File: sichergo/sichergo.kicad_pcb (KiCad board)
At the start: 2 copper layers, 10 parts

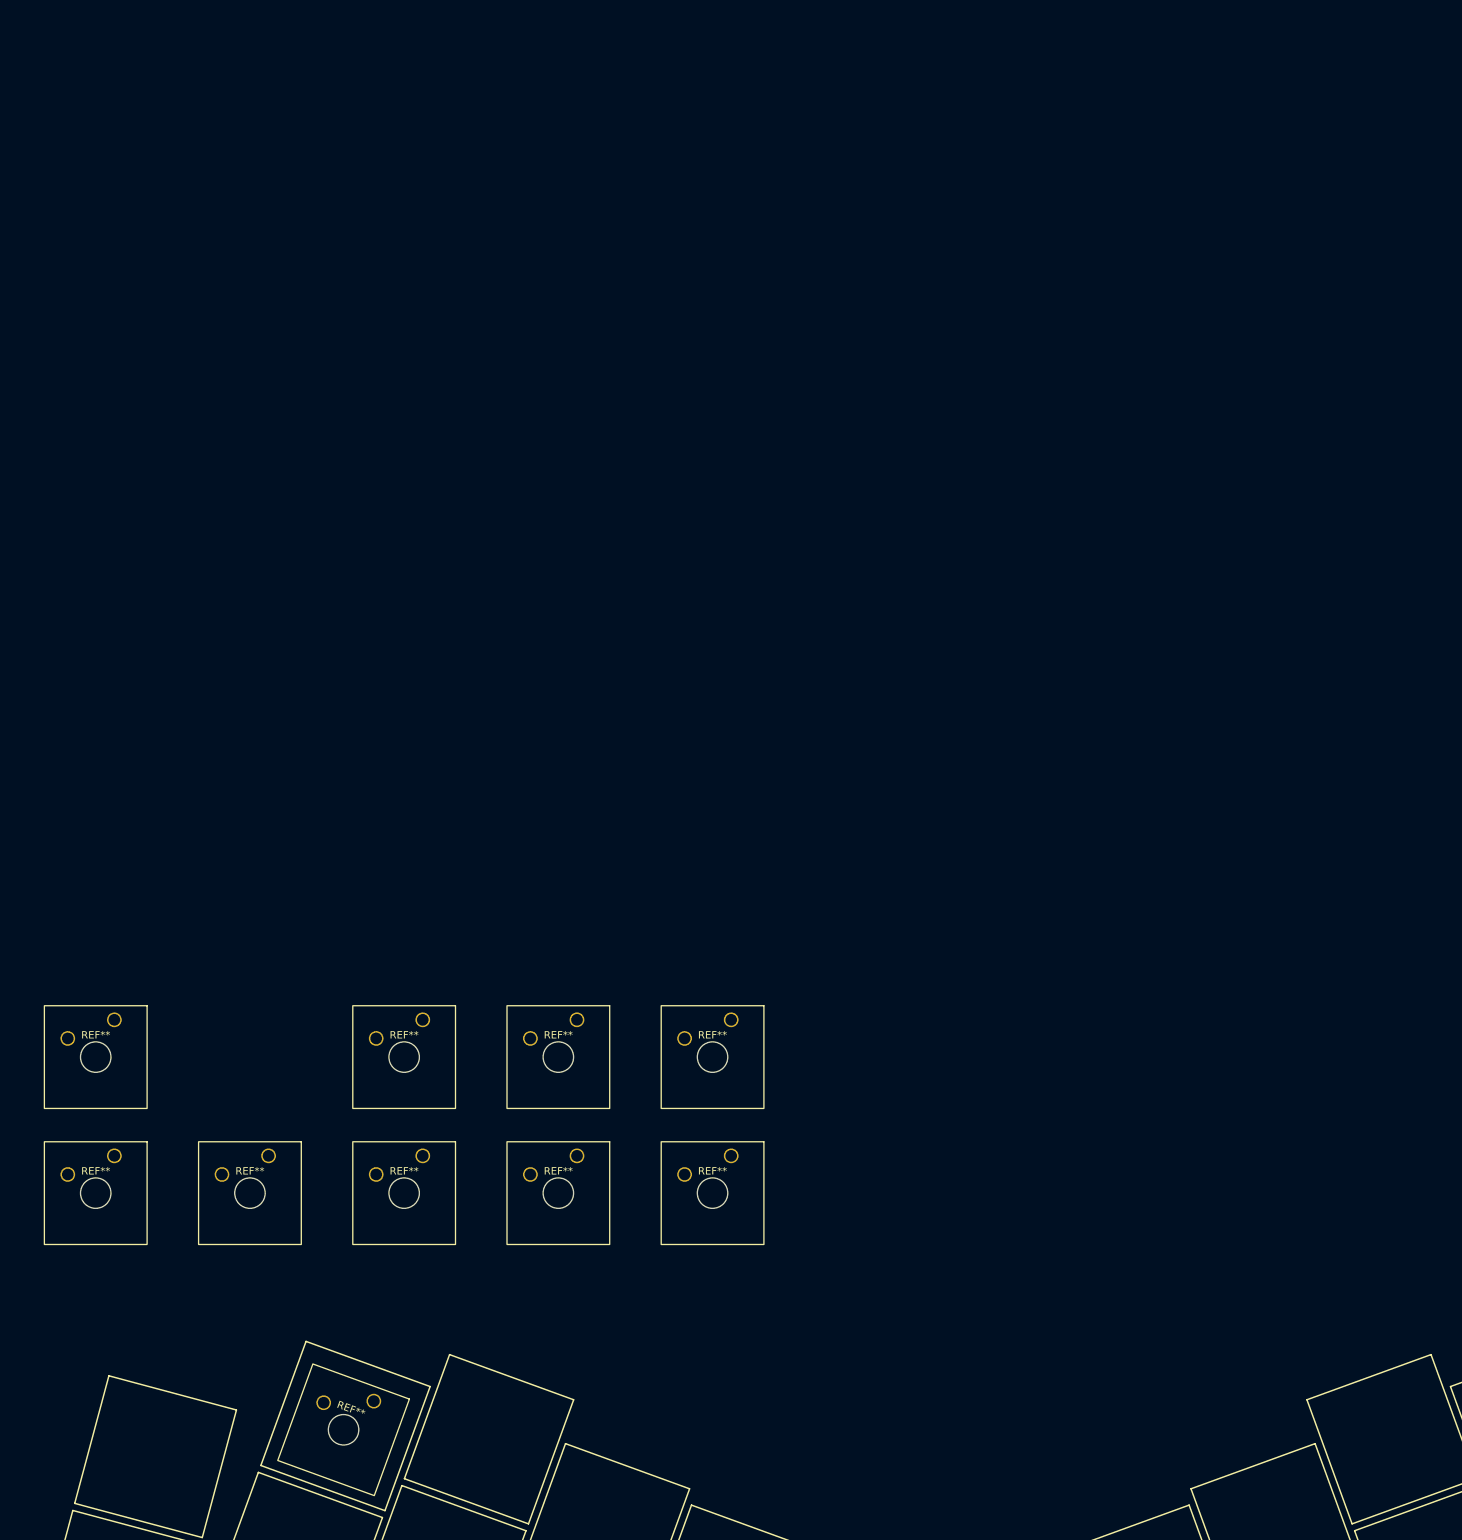
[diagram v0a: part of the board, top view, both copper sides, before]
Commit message: Added footprints to switches
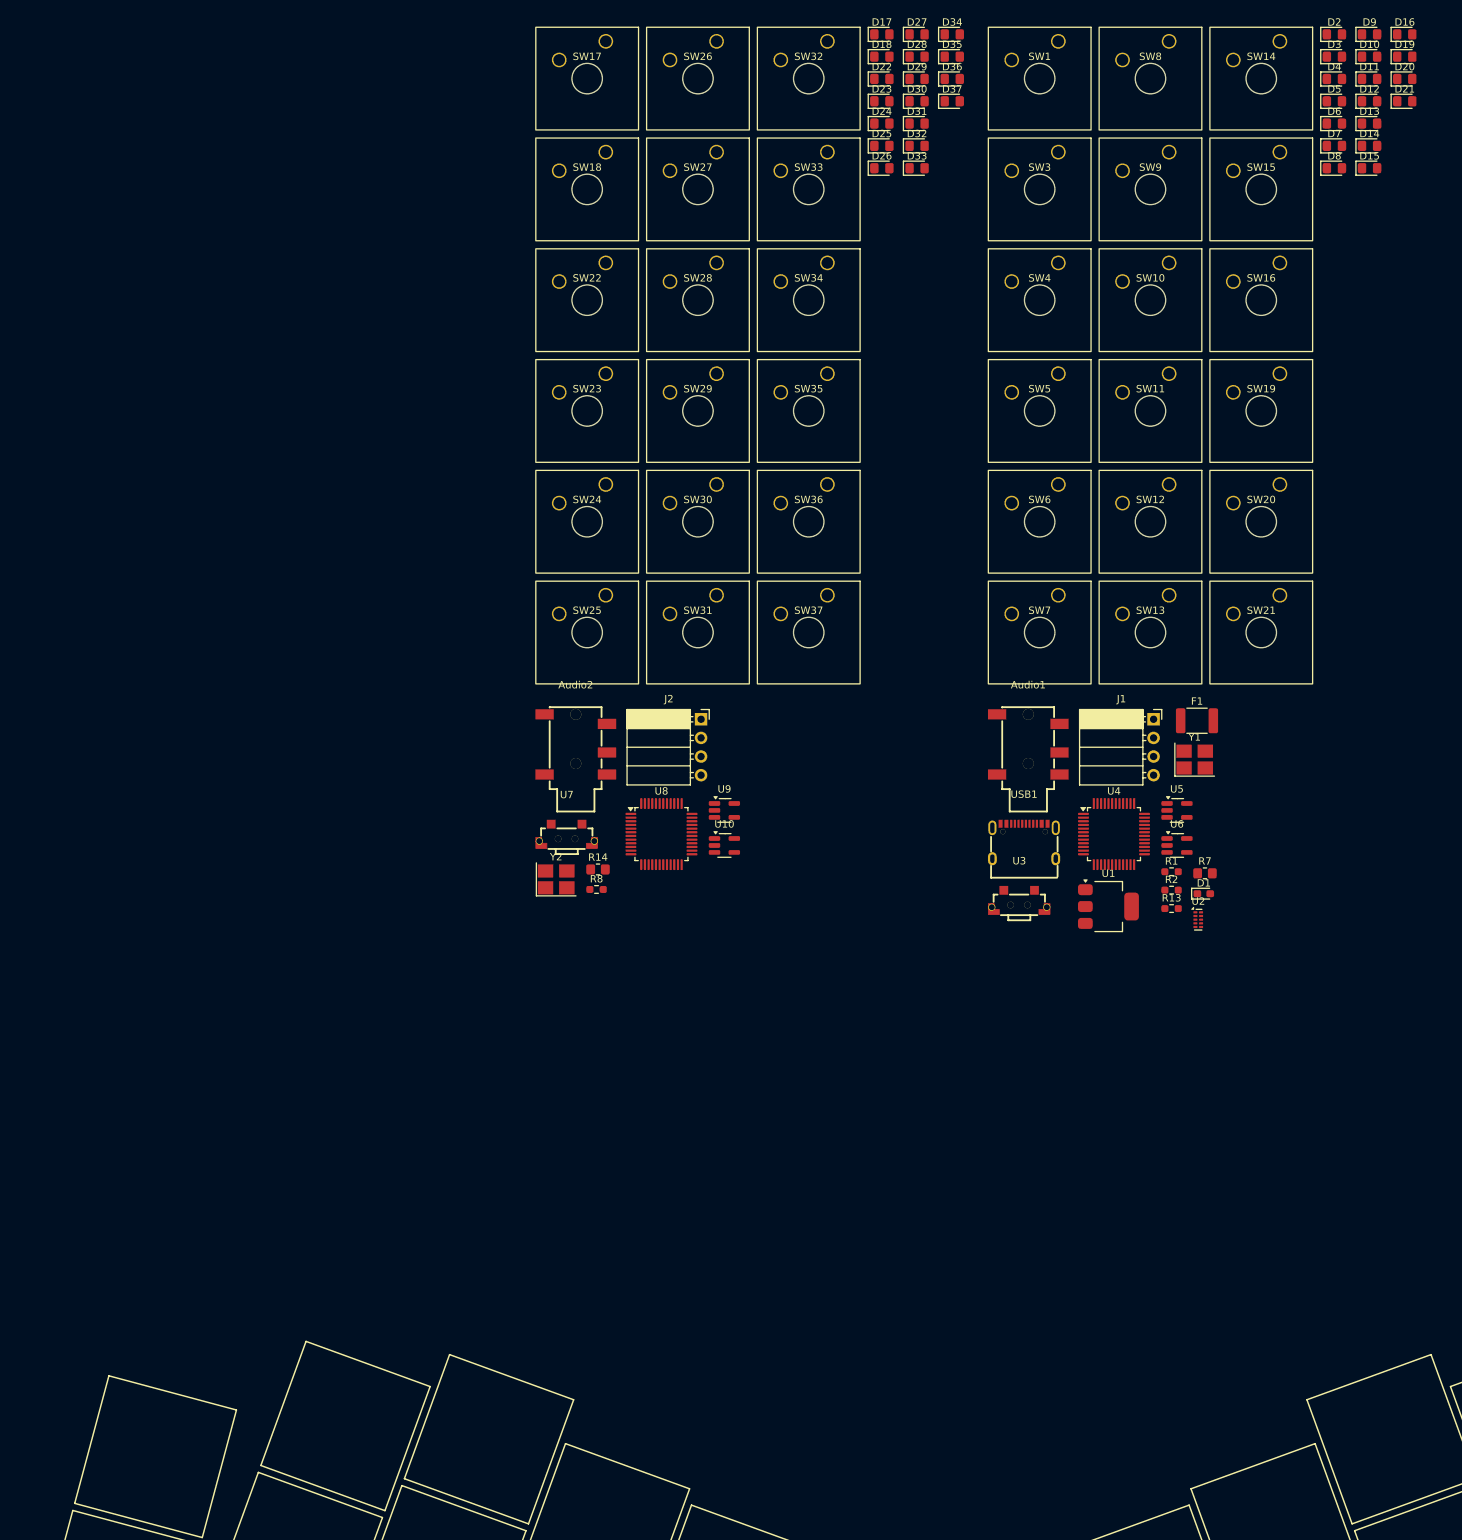
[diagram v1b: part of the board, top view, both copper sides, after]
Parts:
- removed REF** (x10): Gateron_Milky_Yellow, personal:Gateron_Milky_Yellow
- added Audio1: PJ-327E-SMT, easyeda2kicad:AUDIO-SMD_PJ-327E-SMT, F.Cu at (156.7, -28.5)
- added Audio2: PJ-327E-SMT, easyeda2kicad:AUDIO-SMD_PJ-327E-SMT, F.Cu at (95.0, -28.5)
- added D1: CPDUR5V0HE-HF, Diode_SMD:D_0603_1608Metric_Pad1.05x0.95mm_HandSolder, F.Cu at (180.6, -8.12)
- added D10: CD4148W, Diode_SMD:D_0805_2012Metric_Pad1.15x1.40mm_HandSolder, F.Cu at (203.2, -122.2)
- added D11: CD4148W, Diode_SMD:D_0805_2012Metric_Pad1.15x1.40mm_HandSolder, F.Cu at (203.2, -119.2)
- added D12: CD4148W, Diode_SMD:D_0805_2012Metric_Pad1.15x1.40mm_HandSolder, F.Cu at (203.2, -116.1)
- added D13: CD4148W, Diode_SMD:D_0805_2012Metric_Pad1.15x1.40mm_HandSolder, F.Cu at (203.2, -113.1)
- added D14: CD4148W, Diode_SMD:D_0805_2012Metric_Pad1.15x1.40mm_HandSolder, F.Cu at (203.2, -110.0)
- added D15: CD4148W, Diode_SMD:D_0805_2012Metric_Pad1.15x1.40mm_HandSolder, F.Cu at (203.2, -107.0)
- added D16: CD4148W, Diode_SMD:D_0805_2012Metric_Pad1.15x1.40mm_HandSolder, F.Cu at (208.0, -125.2)
- added D17: CD4148W, Diode_SMD:D_0805_2012Metric_Pad1.15x1.40mm_HandSolder, F.Cu at (136.8, -125.2)
- added D18: CD4148W, Diode_SMD:D_0805_2012Metric_Pad1.15x1.40mm_HandSolder, F.Cu at (136.8, -122.2)
- added D19: CD4148W, Diode_SMD:D_0805_2012Metric_Pad1.15x1.40mm_HandSolder, F.Cu at (208.0, -122.2)
- added D2: CD4148W, Diode_SMD:D_0805_2012Metric_Pad1.15x1.40mm_HandSolder, F.Cu at (198.4, -125.2)
- added D20: CD4148W, Diode_SMD:D_0805_2012Metric_Pad1.15x1.40mm_HandSolder, F.Cu at (208.0, -119.2)
- added D21: CD4148W, Diode_SMD:D_0805_2012Metric_Pad1.15x1.40mm_HandSolder, F.Cu at (208.0, -116.1)
- added D22: CD4148W, Diode_SMD:D_0805_2012Metric_Pad1.15x1.40mm_HandSolder, F.Cu at (136.8, -119.2)
- added D23: CD4148W, Diode_SMD:D_0805_2012Metric_Pad1.15x1.40mm_HandSolder, F.Cu at (136.8, -116.1)
- added D24: CD4148W, Diode_SMD:D_0805_2012Metric_Pad1.15x1.40mm_HandSolder, F.Cu at (136.8, -113.1)
- added D25: CD4148W, Diode_SMD:D_0805_2012Metric_Pad1.15x1.40mm_HandSolder, F.Cu at (136.8, -110.0)
- added D26: CD4148W, Diode_SMD:D_0805_2012Metric_Pad1.15x1.40mm_HandSolder, F.Cu at (136.8, -107.0)
- added D27: CD4148W, Diode_SMD:D_0805_2012Metric_Pad1.15x1.40mm_HandSolder, F.Cu at (141.6, -125.2)
- added D28: CD4148W, Diode_SMD:D_0805_2012Metric_Pad1.15x1.40mm_HandSolder, F.Cu at (141.6, -122.2)
- added D29: CD4148W, Diode_SMD:D_0805_2012Metric_Pad1.15x1.40mm_HandSolder, F.Cu at (141.6, -119.2)
- added D3: CD4148W, Diode_SMD:D_0805_2012Metric_Pad1.15x1.40mm_HandSolder, F.Cu at (198.4, -122.2)
- added D30: CD4148W, Diode_SMD:D_0805_2012Metric_Pad1.15x1.40mm_HandSolder, F.Cu at (141.6, -116.1)
- added D31: CD4148W, Diode_SMD:D_0805_2012Metric_Pad1.15x1.40mm_HandSolder, F.Cu at (141.6, -113.1)
- added D32: CD4148W, Diode_SMD:D_0805_2012Metric_Pad1.15x1.40mm_HandSolder, F.Cu at (141.6, -110.0)
- added D33: CD4148W, Diode_SMD:D_0805_2012Metric_Pad1.15x1.40mm_HandSolder, F.Cu at (141.6, -107.0)
- added D34: CD4148W, Diode_SMD:D_0805_2012Metric_Pad1.15x1.40mm_HandSolder, F.Cu at (146.3, -125.2)
- added D35: CD4148W, Diode_SMD:D_0805_2012Metric_Pad1.15x1.40mm_HandSolder, F.Cu at (146.3, -122.2)
- added D36: CD4148W, Diode_SMD:D_0805_2012Metric_Pad1.15x1.40mm_HandSolder, F.Cu at (146.3, -119.2)
- added D37: CD4148W, Diode_SMD:D_0805_2012Metric_Pad1.15x1.40mm_HandSolder, F.Cu at (146.3, -116.1)
- added D4: CD4148W, Diode_SMD:D_0805_2012Metric_Pad1.15x1.40mm_HandSolder, F.Cu at (198.4, -119.2)
- added D5: CD4148W, Diode_SMD:D_0805_2012Metric_Pad1.15x1.40mm_HandSolder, F.Cu at (198.4, -116.1)
- added D6: CD4148W, Diode_SMD:D_0805_2012Metric_Pad1.15x1.40mm_HandSolder, F.Cu at (198.4, -113.1)
- added D7: CD4148W, Diode_SMD:D_0805_2012Metric_Pad1.15x1.40mm_HandSolder, F.Cu at (198.4, -110.0)
- added D8: CD4148W, Diode_SMD:D_0805_2012Metric_Pad1.15x1.40mm_HandSolder, F.Cu at (198.4, -107.0)
- added D9: CD4148W, Diode_SMD:D_0805_2012Metric_Pad1.15x1.40mm_HandSolder, F.Cu at (203.2, -125.2)
- added F1: 1812L050/30PR, Fuse:Fuse_1812_4532Metric_Pad1.30x3.40mm_HandSolder, F.Cu at (179.7, -31.7)
- added J1: Conn_01x04_Pin, Connector_PinSocket_2.54mm:PinSocket_1x04_P2.54mm_Horizontal, F.Cu at (173.8, -31.9)
- added J2: Conn_01x04_Pin, Connector_PinSocket_2.54mm:PinSocket_1x04_P2.54mm_Horizontal, F.Cu at (112.1, -31.9)
- added R1: 5.1 kohm, Resistor_SMD:R_0603_1608Metric_Pad0.98x0.95mm_HandSolder, F.Cu at (176.2, -11.1)
- added R13: 5.1 kohm, Resistor_SMD:R_0603_1608Metric_Pad0.98x0.95mm_HandSolder, F.Cu at (176.2, -6.09)
- added R14: 100 ohm, Resistor_SMD:R_0805_2012Metric_Pad1.20x1.40mm_HandSolder, F.Cu at (98.1, -11.4)
- added R2: 4.7 kohm, Resistor_SMD:R_0603_1608Metric_Pad0.98x0.95mm_HandSolder, F.Cu at (176.2, -8.60)
- added R7: 100 ohm, Resistor_SMD:R_0805_2012Metric_Pad1.20x1.40mm_HandSolder, F.Cu at (180.8, -10.9)
- added R8: 4.7 kohm, Resistor_SMD:R_0603_1608Metric_Pad0.98x0.95mm_HandSolder, F.Cu at (97.9, -8.69)
- added SW1: SW_Push, personal:Gateron_Milky_Yellow, F.Cu at (158.3, -119.2)
- added SW10: SW_Push, personal:Gateron_Milky_Yellow, F.Cu at (173.4, -89.0)
- added SW11: SW_Push, personal:Gateron_Milky_Yellow, F.Cu at (173.4, -73.9)
- added SW12: SW_Push, personal:Gateron_Milky_Yellow, F.Cu at (173.4, -58.8)
- added SW13: SW_Push, personal:Gateron_Milky_Yellow, F.Cu at (173.4, -43.7)
- added SW14: SW_Push, personal:Gateron_Milky_Yellow, F.Cu at (188.5, -119.2)
- added SW15: SW_Push, personal:Gateron_Milky_Yellow, F.Cu at (188.5, -104.1)
- added SW16: SW_Push, personal:Gateron_Milky_Yellow, F.Cu at (188.5, -89.0)
- added SW17: SW_Push, personal:Gateron_Milky_Yellow, F.Cu at (96.6, -119.2)
- added SW18: SW_Push, personal:Gateron_Milky_Yellow, F.Cu at (96.6, -104.1)
- added SW19: SW_Push, personal:Gateron_Milky_Yellow, F.Cu at (188.5, -73.9)
- added SW20: SW_Push, personal:Gateron_Milky_Yellow, F.Cu at (188.5, -58.8)
- added SW21: SW_Push, personal:Gateron_Milky_Yellow, F.Cu at (188.5, -43.7)
- added SW22: SW_Push, personal:Gateron_Milky_Yellow, F.Cu at (96.6, -89.0)
- added SW23: SW_Push, personal:Gateron_Milky_Yellow, F.Cu at (96.6, -73.9)
- added SW24: SW_Push, personal:Gateron_Milky_Yellow, F.Cu at (96.6, -58.8)
- added SW25: SW_Push, personal:Gateron_Milky_Yellow, F.Cu at (96.6, -43.7)
- added SW26: SW_Push, personal:Gateron_Milky_Yellow, F.Cu at (111.7, -119.2)
- added SW27: SW_Push, personal:Gateron_Milky_Yellow, F.Cu at (111.7, -104.1)
- added SW28: SW_Push, personal:Gateron_Milky_Yellow, F.Cu at (111.7, -89.0)
- added SW29: SW_Push, personal:Gateron_Milky_Yellow, F.Cu at (111.7, -73.9)
- added SW3: SW_Push, personal:Gateron_Milky_Yellow, F.Cu at (158.3, -104.1)
- added SW30: SW_Push, personal:Gateron_Milky_Yellow, F.Cu at (111.7, -58.8)
- added SW31: SW_Push, personal:Gateron_Milky_Yellow, F.Cu at (111.7, -43.7)
- added SW32: SW_Push, personal:Gateron_Milky_Yellow, F.Cu at (126.8, -119.2)
- added SW33: SW_Push, personal:Gateron_Milky_Yellow, F.Cu at (126.8, -104.1)
- added SW34: SW_Push, personal:Gateron_Milky_Yellow, F.Cu at (126.8, -89.0)
- added SW35: SW_Push, personal:Gateron_Milky_Yellow, F.Cu at (126.8, -73.9)
- added SW36: SW_Push, personal:Gateron_Milky_Yellow, F.Cu at (126.8, -58.8)
- added SW37: SW_Push, personal:Gateron_Milky_Yellow, F.Cu at (126.8, -43.7)
- added SW4: SW_Push, personal:Gateron_Milky_Yellow, F.Cu at (158.3, -89.0)
- added SW5: SW_Push, personal:Gateron_Milky_Yellow, F.Cu at (158.3, -73.9)
- added SW6: SW_Push, personal:Gateron_Milky_Yellow, F.Cu at (158.3, -58.8)
- added SW7: SW_Push, personal:Gateron_Milky_Yellow, F.Cu at (158.3, -43.7)
- added SW8: SW_Push, personal:Gateron_Milky_Yellow, F.Cu at (173.4, -119.2)
- added SW9: SW_Push, personal:Gateron_Milky_Yellow, F.Cu at (173.4, -104.1)
- added U1: AZ1117-3.3, Package_TO_SOT_SMD:SOT-223-3_TabPin2, F.Cu at (167.6, -6.36)
- added U10: SN74LVC1G125DBV, Package_TO_SOT_SMD:SOT-23-5_HandSoldering, F.Cu at (115.3, -14.7)
- added U2: TPD4E05U06DQA, Package_SON:USON-10_2.5x1.0mm_P0.5mm, F.Cu at (179.9, -4.57)
- added U3: YTS1C0033BBG01, easyeda2kicad:SW-SMD_YIYUAN_YTS1C003XXX, F.Cu at (155.5, -7.29)
- added U4: STM32F103C8Tx, Package_QFP:LQFP-48_7x7mm_P0.5mm, F.Cu at (168.4, -16.2)
- added U5: SN74LVC1G125DBV, Package_TO_SOT_SMD:SOT-23-5_HandSoldering, F.Cu at (177.0, -19.5)
- added U6: SN74LVC1G125DBV, Package_TO_SOT_SMD:SOT-23-5_HandSoldering, F.Cu at (177.0, -14.7)
- added U7: YTS1C0033BBG01, easyeda2kicad:SW-SMD_YIYUAN_YTS1C003XXX, F.Cu at (93.8, -16.3)
- added U8: STM32F103C8Tx, Package_QFP:LQFP-48_7x7mm_P0.5mm, F.Cu at (106.7, -16.2)
- added U9: SN74LVC1G125DBV, Package_TO_SOT_SMD:SOT-23-5_HandSoldering, F.Cu at (115.3, -19.5)
- added USB1: TYPE-C 16PIN 2MD(073), easyeda2kicad:USB-C-SMD_TYPE-C-6PIN-2MD-073, F.Cu at (156.1, -15.3)
- added Y1: Crystal_GND24, Crystal:Crystal_SMD_3225-4Pin_3.2x2.5mm_HandSoldering, F.Cu at (179.4, -26.4)
- added Y2: Crystal_GND24, Crystal:Crystal_SMD_3225-4Pin_3.2x2.5mm_HandSoldering, F.Cu at (92.4, -10.1)

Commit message: Add backlight and switch connections
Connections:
- Audio1 pad 1: +3V3 -> Net-(Audio1-Pad1)
- Audio1 pad 2: Net-(Audio1-Pad2) -> +3V3
- Audio1 pad 5: Net-(Audio1-Pad2) -> +3V3
- Audio2 pad 1: +3V3 -> Net-(Audio2-Pad1)
- Audio2 pad 2: Net-(Audio2-Pad2) -> +3V3
- Audio2 pad 5: Net-(Audio2-Pad2) -> +3V3
- D10 pad 1: /KBD_L/MatrixL/KB_ROW_1 -> /KBD_L/KB_ROW_1
- D11 pad 1: /KBD_L/MatrixL/KB_ROW_1 -> /KBD_L/KB_ROW_1
- D12 pad 1: /KBD_L/MatrixL/KB_ROW_2 -> /KBD_L/KB_ROW_2
- D13 pad 1: /KBD_L/MatrixL/KB_ROW_2 -> /KBD_L/KB_ROW_2
- D14 pad 1: /KBD_L/MatrixL/KB_ROW_2 -> /KBD_L/KB_ROW_2
- D15 pad 1: /KBD_L/MatrixL/KB_ROW_2 -> /KBD_L/KB_ROW_2
- D16 pad 1: /KBD_L/MatrixL/KB_ROW_2 -> /KBD_L/KB_ROW_2
- D17 pad 1: /KBD_R/MatrixR/KB_ROW_4 -> /KBD_R/KB_ROW_4
- D18 pad 1: /KBD_R/MatrixR/KB_COL_5 -> /KBD_R/KB_ROW_5
- D19 pad 1: /KBD_L/MatrixL/KB_ROW_3 -> /KBD_L/KB_ROW_3
- D2 pad 1: /KBD_L/MatrixL/KB_ROW_0 -> /KBD_L/KB_ROW_0
- D20 pad 1: /KBD_L/MatrixL/KB_ROW_3 -> /KBD_L/KB_ROW_3
- D21 pad 1: /KBD_L/MatrixL/KB_ROW_3 -> /KBD_L/KB_ROW_3
- D22 pad 1: /KBD_R/MatrixR/KB_COL_6 -> /KBD_R/KB_ROW_6
- D23 pad 1: /KBD_R/MatrixR/KB_ROW_4 -> /KBD_R/KB_ROW_4
- D24 pad 1: /KBD_R/MatrixR/KB_COL_5 -> /KBD_R/KB_ROW_5
- D25 pad 1: /KBD_R/MatrixR/KB_COL_6 -> /KBD_R/KB_ROW_6
- D26 pad 1: /KBD_R/MatrixR/KB_ROW_4 -> /KBD_R/KB_ROW_4
- D27 pad 1: /KBD_R/MatrixR/KB_COL_5 -> /KBD_R/KB_ROW_5
- D28 pad 1: /KBD_R/MatrixR/KB_COL_6 -> /KBD_R/KB_ROW_6
- D29 pad 1: /KBD_R/MatrixR/KB_COL_7 -> /KBD_R/KB_ROW_7
- D3 pad 1: /KBD_L/MatrixL/KB_ROW_0 -> /KBD_L/KB_ROW_0
- D30 pad 1: /KBD_R/MatrixR/KB_ROW_4 -> /KBD_R/KB_ROW_4
- D31 pad 1: /KBD_R/MatrixR/KB_COL_5 -> /KBD_R/KB_ROW_5
- D32 pad 1: /KBD_R/MatrixR/KB_COL_6 -> /KBD_R/KB_ROW_6
- D33 pad 1: /KBD_R/MatrixR/KB_COL_7 -> /KBD_R/KB_ROW_7
- D34 pad 1: /KBD_R/MatrixR/KB_ROW_4 -> /KBD_R/KB_ROW_4
- D35 pad 1: /KBD_R/MatrixR/KB_COL_5 -> /KBD_R/KB_ROW_5
- D36 pad 1: /KBD_R/MatrixR/KB_COL_6 -> /KBD_R/KB_ROW_6
- D37 pad 1: /KBD_R/MatrixR/KB_COL_7 -> /KBD_R/KB_ROW_7
- D4 pad 1: /KBD_L/MatrixL/KB_ROW_0 -> /KBD_L/KB_ROW_0
- D5 pad 1: /KBD_L/MatrixL/KB_ROW_0 -> /KBD_L/KB_ROW_0
- D6 pad 1: /KBD_L/MatrixL/KB_ROW_0 -> /KBD_L/KB_ROW_0
- D7 pad 1: /KBD_L/MatrixL/KB_ROW_1 -> /KBD_L/KB_ROW_1
- D8 pad 1: /KBD_L/MatrixL/KB_ROW_1 -> /KBD_L/KB_ROW_1
- D9 pad 1: /KBD_L/MatrixL/KB_ROW_1 -> /KBD_L/KB_ROW_1
- R14 pad 1: Net-(Audio2-Pad2) -> Net-(Audio2-Pad1)
- R7 pad 1: Net-(Audio1-Pad2) -> Net-(Audio1-Pad1)
- SW1 pad 1: /KBD_L/MatrixL/KB_COL_0 -> /KBD_L/KB_COL_0
- SW10 pad 1: /KBD_L/MatrixL/KB_COL_3 -> /KBD_L/KB_COL_3
- SW11 pad 1: /KBD_L/MatrixL/KB_COL_4 -> /KBD_L/KB_COL_4
- SW12 pad 1: /KBD_L/MatrixL/KB_COL_0 -> /KBD_L/KB_COL_0
- SW13 pad 1: /KBD_L/MatrixL/KB_COL_1 -> /KBD_L/KB_COL_1
- SW14 pad 1: /KBD_L/MatrixL/KB_COL_2 -> /KBD_L/KB_COL_2
- SW15 pad 1: /KBD_L/MatrixL/KB_COL_3 -> /KBD_L/KB_COL_3
- SW16 pad 1: /KBD_L/MatrixL/KB_COL_4 -> /KBD_L/KB_COL_4
- SW17 pad 1: /KBD_R/MatrixR/KB_COL_0 -> /KBD_R/KB_COL_0
- SW18 pad 1: /KBD_R/MatrixR/KB_COL_0 -> /KBD_R/KB_COL_0
- SW19 pad 1: /KBD_L/MatrixL/KB_COL_2 -> /KBD_L/KB_COL_2
- SW20 pad 1: /KBD_L/MatrixL/KB_COL_3 -> /KBD_L/KB_COL_3
- SW21 pad 1: /KBD_L/MatrixL/KB_COL_4 -> /KBD_L/KB_COL_4
- SW22 pad 1: /KBD_R/MatrixR/KB_COL_0 -> /KBD_R/KB_COL_0
- SW23 pad 1: /KBD_R/MatrixR/KB_COL_1 -> /KBD_R/KB_COL_1
- SW24 pad 1: /KBD_R/MatrixR/KB_COL_1 -> /KBD_R/KB_COL_1
- SW25 pad 1: /KBD_R/MatrixR/KB_COL_1 -> /KBD_R/KB_COL_1
- SW26 pad 1: /KBD_R/MatrixR/KB_COL_2 -> /KBD_R/KB_COL_2
- SW27 pad 1: /KBD_R/MatrixR/KB_COL_2 -> /KBD_R/KB_COL_2
- SW28 pad 1: /KBD_R/MatrixR/KB_COL_2 -> /KBD_R/KB_COL_2
- SW29 pad 1: /KBD_R/MatrixR/KB_COL_0 -> /KBD_R/KB_COL_0
- SW3 pad 1: /KBD_L/MatrixL/KB_COL_1 -> /KBD_L/KB_COL_1
- SW30 pad 1: /KBD_R/MatrixR/KB_COL_3 -> /KBD_R/KB_COL_3
- SW31 pad 1: /KBD_R/MatrixR/KB_COL_3 -> /KBD_R/KB_COL_3
- SW32 pad 1: /KBD_R/MatrixR/KB_COL_3 -> /KBD_R/KB_COL_3
- SW33 pad 1: /KBD_R/MatrixR/KB_COL_1 -> /KBD_R/KB_COL_1
- SW34 pad 1: /KBD_R/MatrixR/KB_COL_4 -> /KBD_R/KB_COL_4
- SW35 pad 1: /KBD_R/MatrixR/KB_COL_4 -> /KBD_R/KB_COL_4
- SW36 pad 1: /KBD_R/MatrixR/KB_COL_4 -> /KBD_R/KB_COL_4
- SW37 pad 1: /KBD_R/MatrixR/KB_COL_2 -> /KBD_R/KB_COL_2
- SW4 pad 1: /KBD_L/MatrixL/KB_COL_2 -> /KBD_L/KB_COL_2
- SW5 pad 1: /KBD_L/MatrixL/KB_COL_3 -> /KBD_L/KB_COL_3
- SW6 pad 1: /KBD_L/MatrixL/KB_COL_4 -> /KBD_L/KB_COL_4
- SW7 pad 1: /KBD_L/MatrixL/KB_COL_0 -> /KBD_L/KB_COL_0
- SW8 pad 1: /KBD_L/MatrixL/KB_COL_1 -> /KBD_L/KB_COL_1
- SW9 pad 1: /KBD_L/MatrixL/KB_COL_2 -> /KBD_L/KB_COL_2
- U4 pad 10: unconnected-(U4-PA0-Pad10) -> /KBD_L/KB_COL_0
- U4 pad 11: unconnected-(U4-PA1-Pad11) -> /KBD_L/KB_COL_1
- U4 pad 12: unconnected-(U4-PA2-Pad12) -> /KBD_L/KB_COL_2
- U4 pad 13: unconnected-(U4-PA3-Pad13) -> /KBD_L/KB_COL_3
- U4 pad 14: unconnected-(U4-PA4-Pad14) -> /KBD_L/KB_COL_4
- U4 pad 15: unconnected-(U4-PA5-Pad15) -> /KBD_L/KB_ROW_0
- U4 pad 16: unconnected-(U4-PA6-Pad16) -> /KBD_L/KB_ROW_1
- U4 pad 17: unconnected-(U4-PA7-Pad17) -> /KBD_L/KB_ROW_2
- U4 pad 29: unconnected-(U4-PA8-Pad29) -> /KBD_L/KB_ROW_3
- U8 pad 10: unconnected-(U8-PA0-Pad10) -> /KBD_R/KB_COL_0
- U8 pad 11: unconnected-(U8-PA1-Pad11) -> /KBD_R/KB_COL_1
- U8 pad 12: unconnected-(U8-PA2-Pad12) -> /KBD_R/KB_COL_2
- U8 pad 13: unconnected-(U8-PA3-Pad13) -> /KBD_R/KB_COL_3
- U8 pad 14: unconnected-(U8-PA4-Pad14) -> /KBD_R/KB_COL_4
- U8 pad 15: unconnected-(U8-PA5-Pad15) -> /KBD_R/KB_ROW_4
- U8 pad 16: unconnected-(U8-PA6-Pad16) -> /KBD_R/KB_ROW_5
- U8 pad 17: unconnected-(U8-PA7-Pad17) -> /KBD_R/KB_ROW_6
- U8 pad 29: unconnected-(U8-PA8-Pad29) -> /KBD_R/KB_ROW_7
